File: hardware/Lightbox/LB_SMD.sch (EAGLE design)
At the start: 36 parts, among them Q1 8MHz, Q2 IRLZ44Z, Q3 IRLZ44Z, Q4 IRLZ44Z, SW1 NT-10 SMD, U1 ATTiny2313, U2 75176, U3 LM1117-5.0

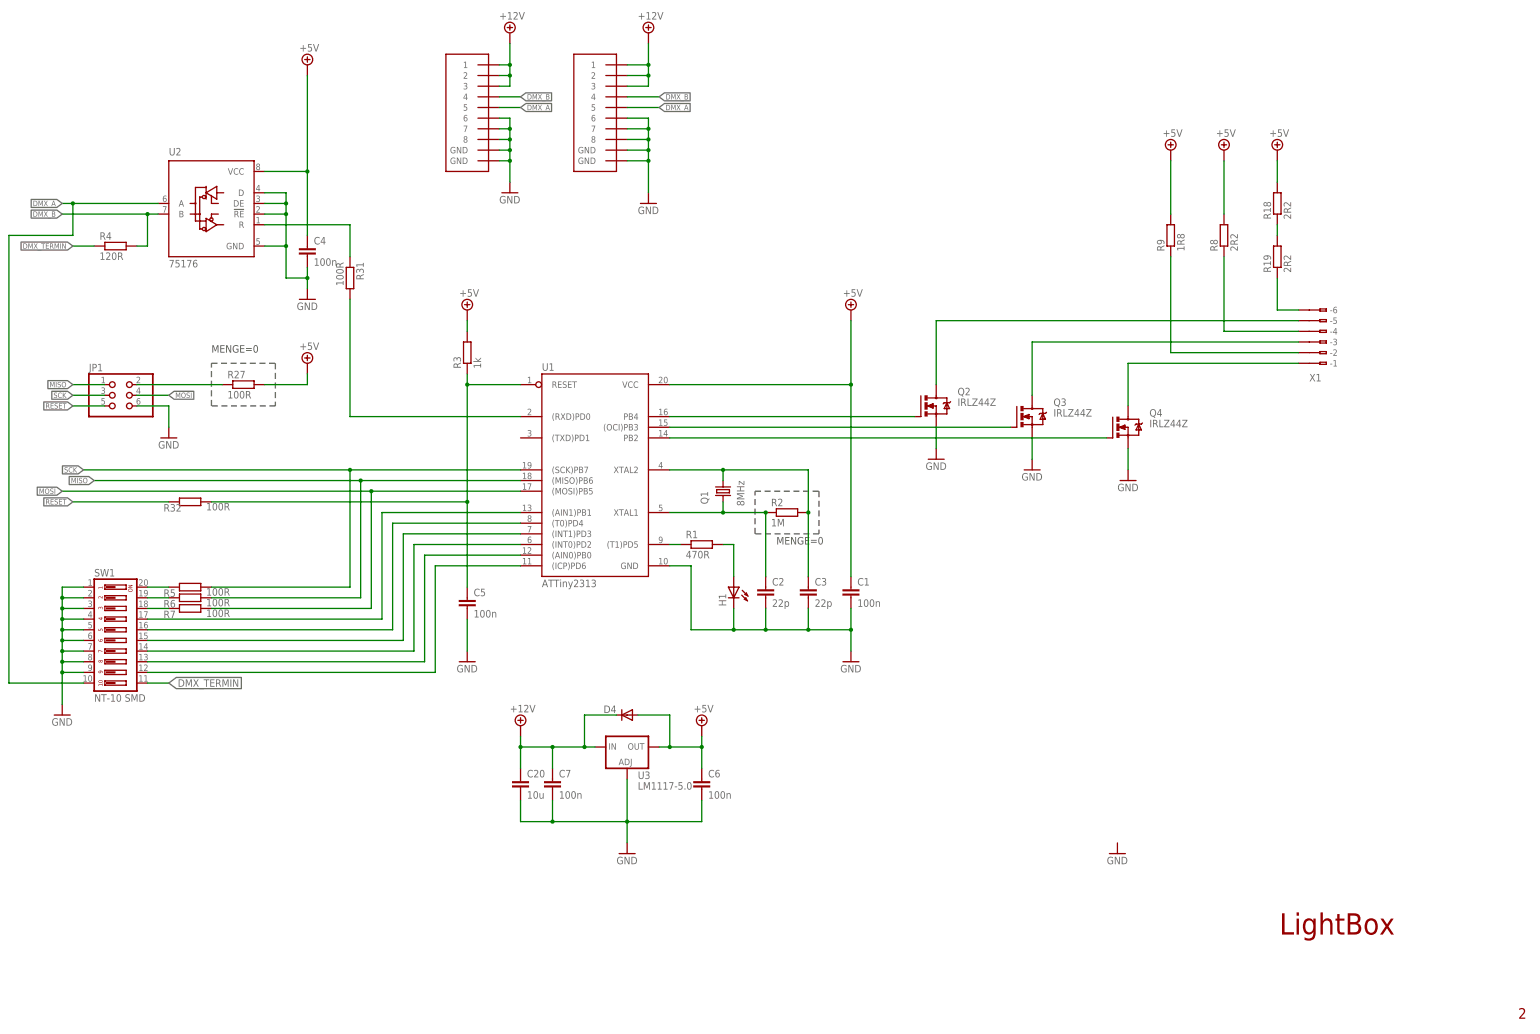
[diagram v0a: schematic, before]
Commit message: changes towards THT layout
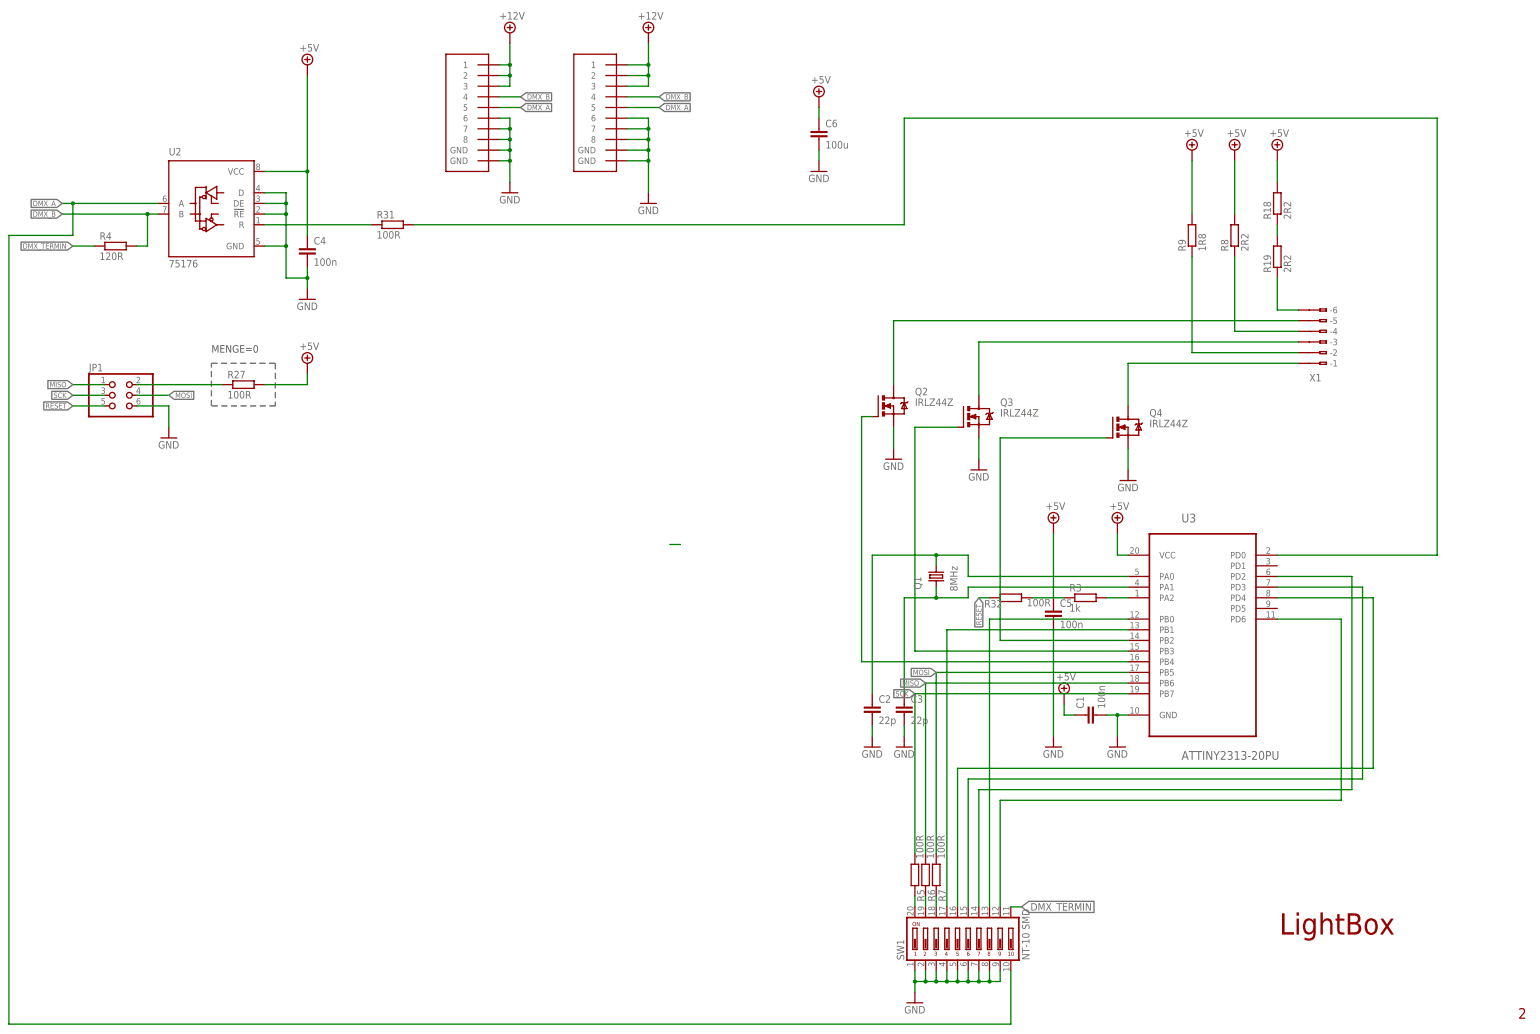
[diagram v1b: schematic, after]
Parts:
- removed C20: 10u, LB:C-1210
- removed C7: 100n, rcl:C-EUC0805
- removed D4: (no value), diode:DIODE-SOD323-W
- removed H1: (no value), led:LEDCHIP-LED0805
- removed R1: 470R, rcl:R-EU_R0805
- removed R2: 1M, rcl:R-EU_R0805
- removed U1: ATTiny2313, LB:AT90S2313S
- C6: value 100n -> 100u
- U3: value LM1117-5.0 -> ATTINY2313-20PU; device v-reg:LM317MBSTT3 -> lightbox:ATTINY2313-20PU
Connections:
- removed net N$1: R1.1, U1.(T1)PD5
- removed net N$18: SW1.12, U1.(ICP)PD6
- removed net N$33: Q2.G, U1.PB4
- removed net N$53: R31.2, U1.(RXD)PD0
- new net N$26: Q2.G, U3.PB4
- new net N$27: C2.1, Q1.1, U3.PA0
- new net N$29: C3.1, Q1.2, U3.PA1
- net +12V: no longer C20.1, C7.1, D4.C, U3.IN
- net +5V: now also R3.1, U3.VCC; no longer D4.A, R3.2, U1.VCC, U3.OUT
- net GND: now also U3.GND; no longer C20.2, C7.2, H1.C, U1.GND, U3.ADJ
- net MISO: now also U3.PB6; no longer U1.(MISO)PB6
- net MOSI: now also U3.PB5; no longer U1.(MOSI)PB5
- net N$11: now also U3.PB3; no longer U1.(OCI)PB3
- net N$13: now also U3.PB1; no longer U1.(AIN1)PB1
- net N$14: now also U3.PD4; no longer U1.(T0)PD4
- net N$15: now also U3.PD3; no longer U1.(INT1)PD3
- net N$16: now also U3.PD2; no longer U1.(INT0)PD2
- net N$17: now also U3.PD0; no longer SW1.13, U1.(AIN0)PB0
- net N$19: now also U3.PB2; no longer U1.PB2
- net N$2: now also R3.2, U3.PA2; no longer C2.1, Q1.2, R2.1, U1.XTAL1
- net N$3: now also SW1.12, U3.PD6; no longer H1.A, R1.2
- net N$4: now also SW1.13, U3.PB0; no longer C3.1, Q1.1, R2.2, U1.XTAL2
- net N$6: no longer R3.1, U1.RESET
- net SCK: now also U3.PB7; no longer U1.(SCK)PB7
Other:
- moved on the sheet: C1, C2, C3, C5, C6, Q1, Q2, Q3, R3, R31, R32, R5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
